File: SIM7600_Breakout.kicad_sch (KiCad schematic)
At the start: 60 parts, among them J1 SIM8060-6-0-14-00-A, J2 2W Header, J3 MJ-3502N, J4 30W Header, J5 USB_B_Micro, J6 U.FL-R-SMT-1(01), J7 U.FL-R-SMT-1(01), J8 U.FL-R-SMT-1(01), Q1 MMBT3904L_RFG, U1 NVT2008PW_118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

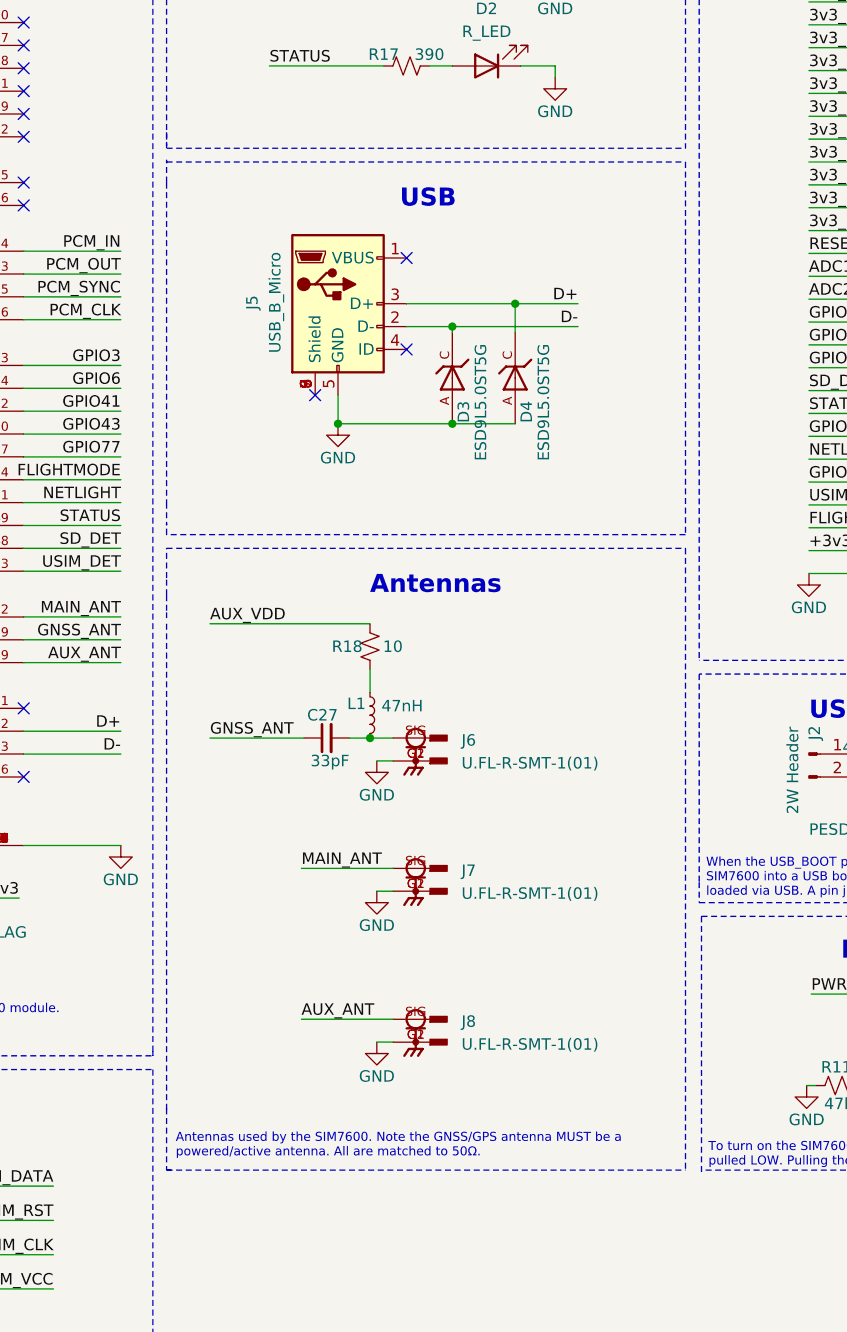
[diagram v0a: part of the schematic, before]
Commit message: Added USB C to schematic & half assed putting it on the PCB
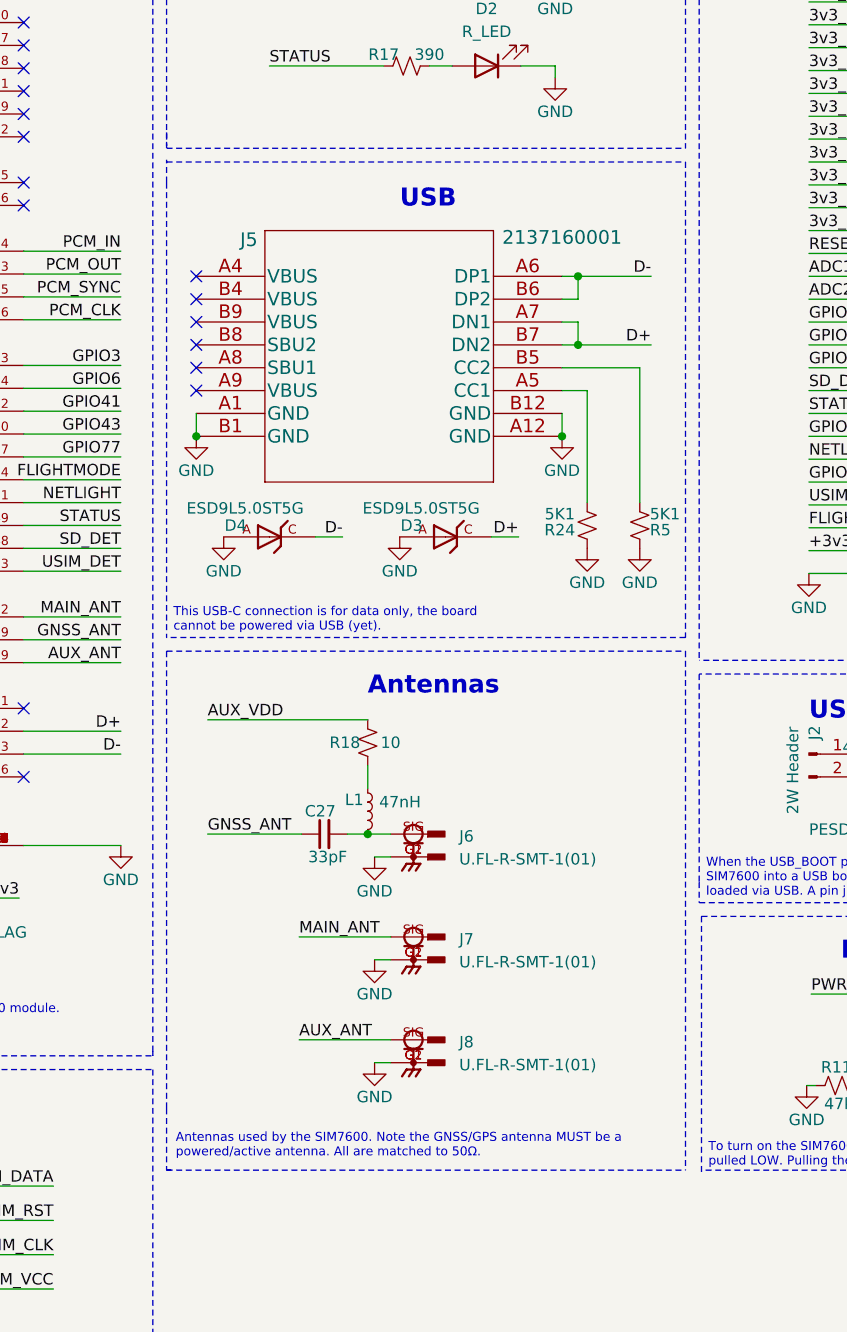
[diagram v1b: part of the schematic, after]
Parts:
- removed J5: USB_B_Micro, sim7600_breakout:USB3100-30-A, symbol Connector:USB_B_Micro
- added J5: 2137160001, sim7600_breakout:2137160001-USB-C, symbol 2137160001-USB-C:2137160001
- added R24, R5: 5K1, Resistor_SMD:R_0201_0603Metric_Pad0.64x0.40mm_HandSolder, symbol Device:R_Small_US
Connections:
- net D+: now also D3.C, J5.A7 (DN1), J5.B7 (DN2); no longer D4.C
- net D-: now also D4.C, J5.A6 (DP1), J5.B6 (DP2); no longer D3.C
- net GND: now also J5.A1 (GND), J5.A12 (GND), J5.B1 (GND), J5.B12 (GND), R24.1, R5.1
- new net: J5.B5 (CC2), R5.2
- new net: J5.A5 (CC1), R24.2
- no-connect marks 27 -> 30
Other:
- note added: "This USB-C connection is for data only, the board cannot be powered via USB (yet)."
- moved on the sheet: C27, D3, D4, J6, J7, J8, L1, R18
